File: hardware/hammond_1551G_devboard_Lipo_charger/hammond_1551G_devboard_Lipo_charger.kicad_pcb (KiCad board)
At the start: 4 copper layers, 44 x 29 mm, 25 parts, among them J1 DevBoardDigital, J2 DevBoardAnalog, J3 Battery_2pin, J4 DevBoardUartInput, J5 JTAG_2X05, Q1 Q_NMOS_GSD, U1 MCP1702-MB, U2 power_joiner_2_nets, U3 power_joiner_2_nets, U4 power_joiner_2_nets, U5 power_joiner_2_nets, U6 MCP738312-OT

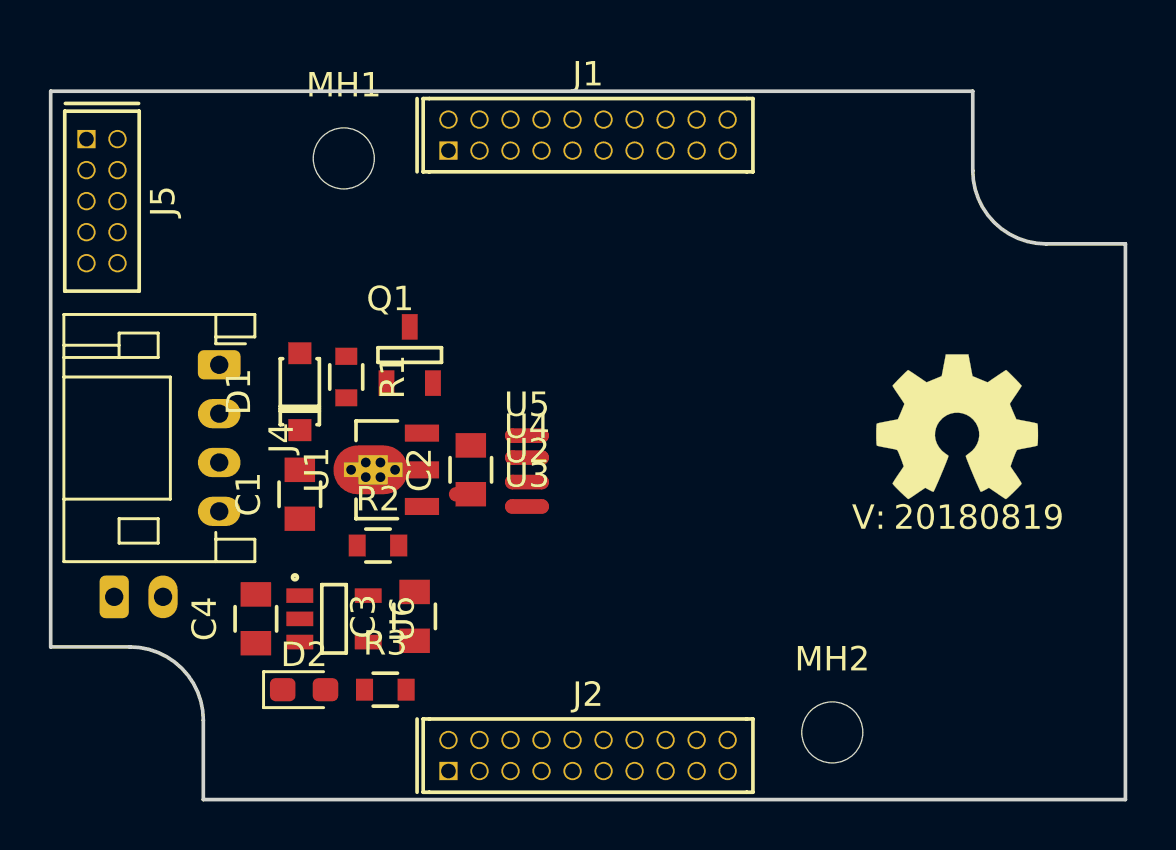
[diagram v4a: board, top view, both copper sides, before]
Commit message: further placement/layout, included newer PCB library
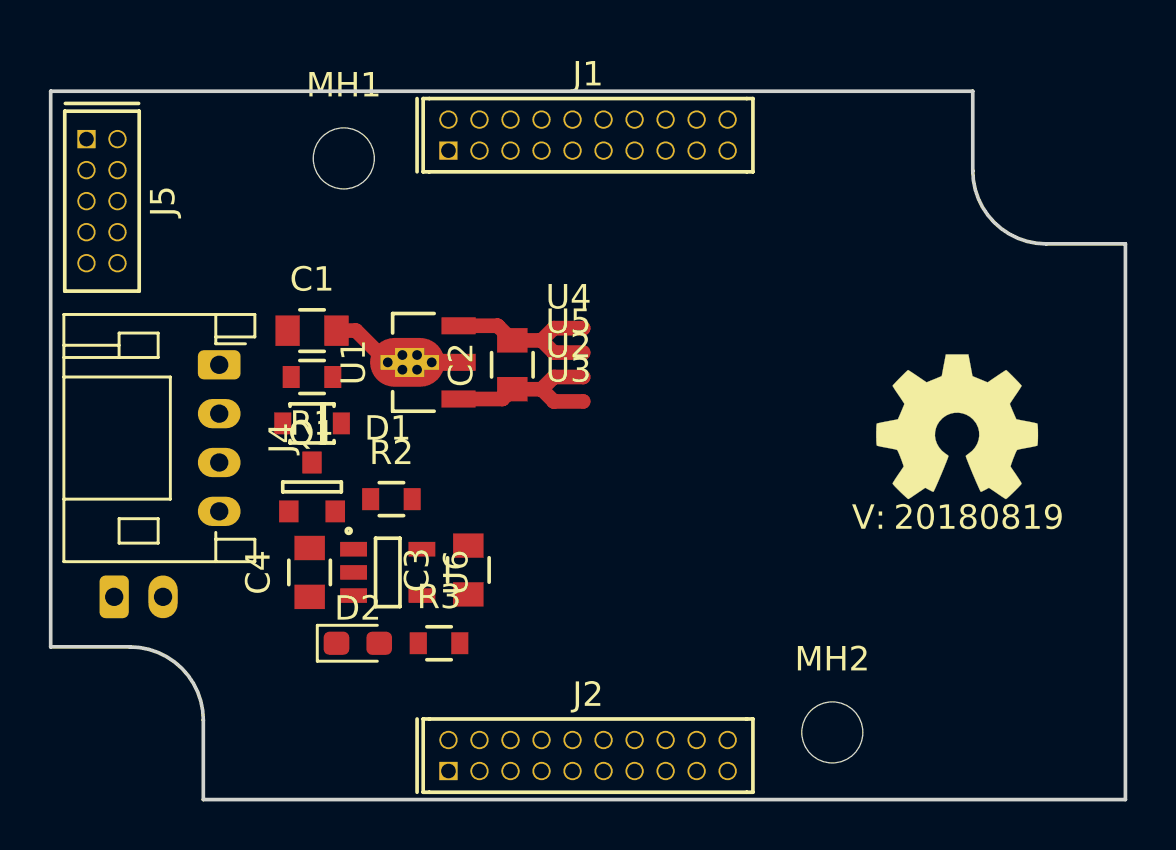
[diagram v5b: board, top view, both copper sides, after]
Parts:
- D1: footprint SquantorDiodes:SOD-123 -> SquantorDiodes:SOD_323_onsemi
- Q1: footprint SquantorIC:SOT23-3-Microchip-TT -> SquantorIC:SOT23-3
- moved Q1 6.72 mm to (49.0, 164.5)
- moved C1 6.72 mm to (49.0, 158.1), turned to 0 degrees
- moved U4 5.57 mm to (59.5, 158.0)
- moved U1 4.65 mm to (55.0, 159.4)
- moved C2 4.62 mm to (57.2, 159.5)
- moved U2 4.62 mm to (59.5, 160.0)
- moved U3 4.62 mm to (59.5, 161.0)
- moved U5 3.80 mm to (59.5, 159.0)
- moved D2 2.91 mm to (50.9, 170.9)
- moved R3 2.91 mm to (54.2, 170.9)
- moved U6 2.91 mm to (52.1, 168.0)
- moved C3 2.91 mm to (55.4, 167.9)
- moved C4 2.91 mm to (48.9, 168.0)
- moved R2 1.98 mm to (52.2, 165.0)
- moved R1 1.40 mm to (49.0, 160.0), turned to 180 degrees
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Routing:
- net Net-(C2-Pad2): track 0.00 -> 5.06 mm
- net Net-(C1-Pad2): track 0.00 -> 4.74 mm
- net GND: track 0.60 -> 4.98 mm

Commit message: completed layout, time for silk screen updates
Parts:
- moved U4 8.71 mm to (54.9, 165.4)
- moved U2 7.88 mm to (54.9, 166.4)
- moved U3 7.88 mm to (54.9, 167.4)
- moved U5 7.09 mm to (54.9, 164.4)
- moved R3 5.42 mm to (49.2, 173.0), turned to 90 degrees
- moved C2 5.33 mm to (53.1, 162.9), turned to 0 degrees
- moved C4 4.16 mm to (45.2, 169.9)
- moved D2 4.15 mm to (47.3, 173.0), turned to 270 degrees
- moved R2 4.07 mm to (48.7, 167.0), turned to 180 degrees
- moved C3 3.99 mm to (51.7, 169.4)
- moved U6 3.90 mm to (48.5, 169.5)
- moved U1 2.22 mm to (53.2, 160.7), turned to 0 degrees
- moved R1 0.30 mm to (48.7, 160.0)
- moved Q1 0.10 mm to (49.0, 164.4), turned to 90 degrees
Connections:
- net Net-(C1-Pad2) renamed /VREG
- J5 pad 1: GND -> VSS
- J5 pad 3: GND -> VSS
- J5 pad 5: GND -> VSS
- J5 pad 9: GND -> VSS
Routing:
- net +BATT: track 0.00 -> 36.1 mm, vias 0 -> 2
- net VBUS: track 0.00 -> 29.4 mm
- net GND: track 4.98 -> 24.5 mm, vias 0 -> 2
- net VDD: track 0.00 -> 17.0 mm
- net VDDA: track 0.00 -> 11.9 mm, vias 0 -> 1
- net VSSA: track 0.00 -> 11.3 mm
- net /VREG: track 4.74 -> 11.1 mm
- net Net-(D2-Pad1): track 0.00 -> 4.98 mm
- net Net-(J4-Pad3): track 0.00 -> 4.25 mm
- net VSS: track 0.00 -> 4.07 mm, vias 0 -> 1
- net Net-(D2-Pad2): track 0.00 -> 1.91 mm
- net Net-(R2-Pad1): track 0.00 -> 1.69 mm
- added copper zone on B.Cu, net /VREG
- added copper zone on B.Cu, net GND
- added copper zone on B.Cu, net VSS
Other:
- copper layers 4 -> 2
- net class Default: clearance 0.127 -> 0.1527; trace_width 0.127 -> 0.1527
- rule trace_clearance: 0.127 -> 0.1527
- rule trace_min: 0.127 -> 0.1524

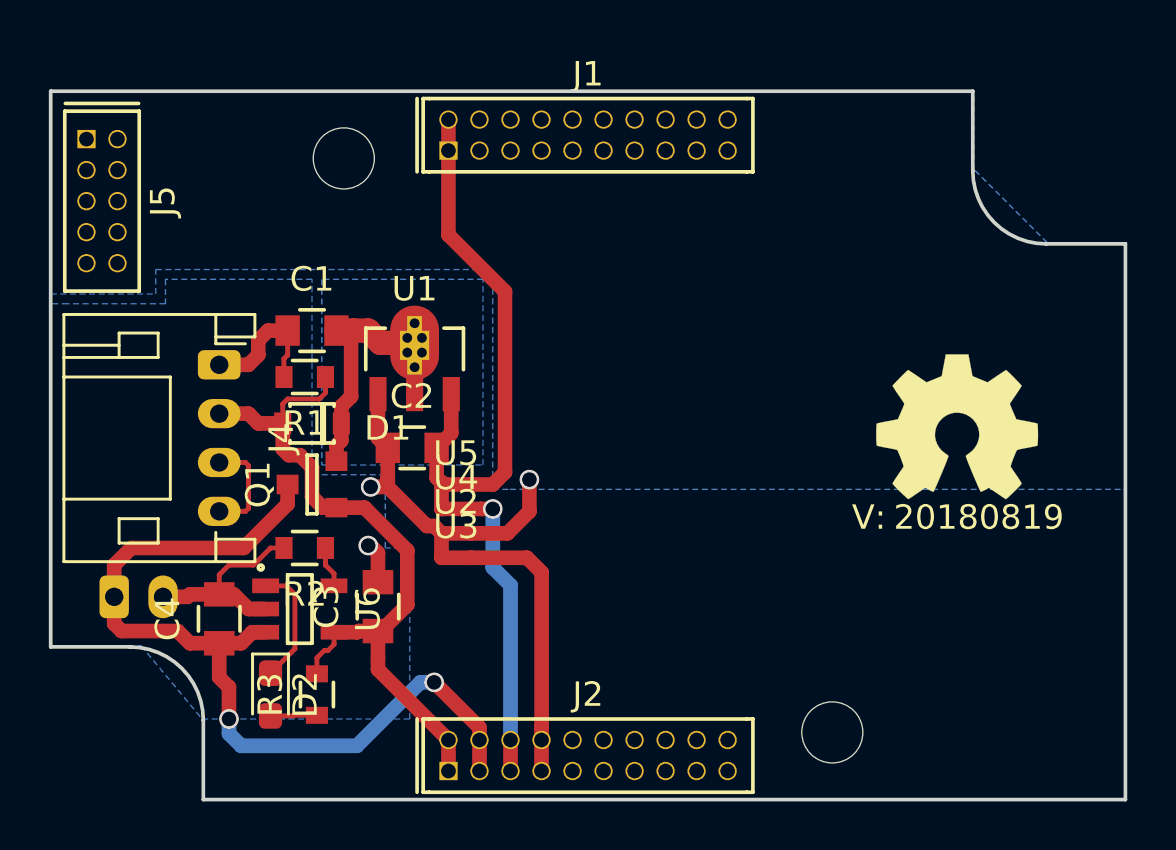
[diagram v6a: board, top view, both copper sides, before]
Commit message: replaced JST PH connectors by SMD variants so they stack better, needed to redo layout altough :(
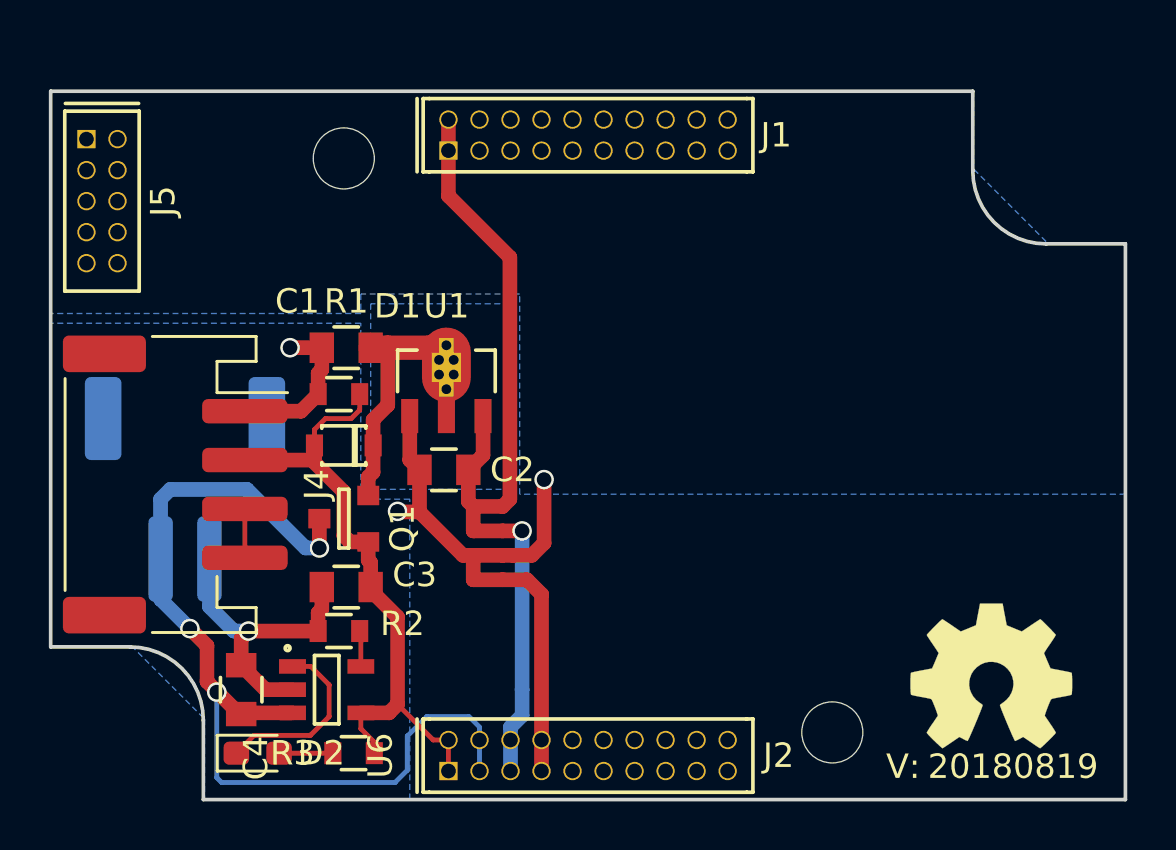
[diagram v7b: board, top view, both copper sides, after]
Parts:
- J3: footprint Connector_JST:JST_PH_S2B-PH-K_1x02_P2.00mm_Horizontal -> Connector_JST:JST_PH_S2B-PH-SM4-TB_1x02-1MP_P2.00mm_Horizontal
- J4: footprint Connector_JST:JST_PH_S4B-PH-K_1x04_P2.00mm_Horizontal -> Connector_JST:JST_PH_S4B-PH-SM4-TB_1x04-1MP_P2.00mm_Horizontal
- moved N2 10.3 mm to (78.1, 176.1)
- moved N1 10.3 mm to (76.8, 172.2)
- moved J3 5.27 mm to (43.8, 164.6)
- moved J4 5.22 mm to (43.4, 164.4)
- moved R2 3.68 mm to (50.1, 170.4)
- moved U6 3.48 mm to (49.6, 172.8)
- moved C4 3.04 mm to (46.1, 172.8)
- moved R3 2.83 mm to (50.7, 175.4), turned to 0 degrees
- moved D2 2.46 mm to (46.8, 175.4), turned to 0 degrees
- moved Q1 1.91 mm to (50.3, 165.8)
- moved U2 1.58 mm to (56.2, 167.3)
- moved U3 1.58 mm to (56.2, 168.3)
- moved U4 1.58 mm to (56.2, 166.3)
- moved U5 1.58 mm to (56.2, 165.3)
- moved C2 1.58 mm to (54.4, 163.8)
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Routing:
- net GND: track 24.5 -> 28.2 mm, vias 2 -> 3
- net +BATT: track 36.1 -> 39.5 mm, vias 2 -> 3
- net VBUS: track 29.4 -> 26.2 mm
- net Net-(D2-Pad1): track 4.98 -> 7.53 mm
- net Net-(J4-Pad3): track 4.25 -> 2.00 mm
- net VSSA: track 11.3 -> 9.08 mm
- net VDDA: track 11.9 -> 10.8 mm
- net Net-(D2-Pad2): track 1.91 -> 2.48 mm

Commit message: finished layout of an additional JTAG connection
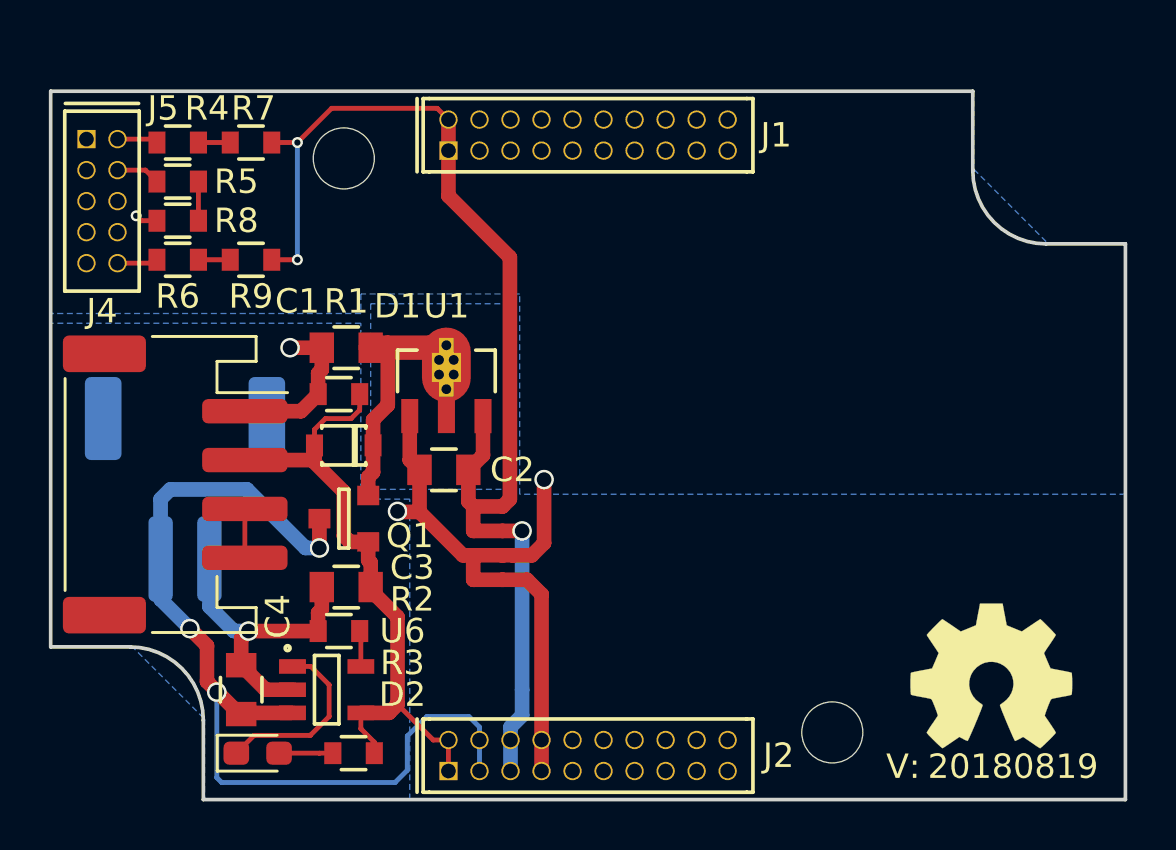
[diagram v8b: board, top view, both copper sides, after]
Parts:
- added R4: 100, SquantorRcl:R_0603_hand, F.Cu at (43.5, 150.4)
- added R5: 100, SquantorRcl:R_0603_hand, F.Cu at (43.5, 152.0)
- added R6: 100, SquantorRcl:R_0603_hand, F.Cu at (43.5, 155.2)
- added R7: 100k, SquantorRcl:R_0603_hand, F.Cu at (46.5, 150.4)
- added R8: 100k, SquantorRcl:R_0603_hand, F.Cu at (43.5, 153.6)
- added R9: 100k, SquantorRcl:R_0603_hand, F.Cu at (46.5, 155.2)
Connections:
- J5 pad 10: (no net) -> Net-(J5-Pad10)
- J5 pad 2: (no net) -> Net-(J5-Pad2)
- J5 pad 4: (no net) -> Net-(J5-Pad4)
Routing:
- net VDD: track 17.0 -> 30.9 mm, vias 0 -> 2
- net Net-(J5-Pad4): track 0.00 -> 1.81 mm
- net Net-(J5-Pad2): track 0.00 -> 1.67 mm
- net Net-(J5-Pad10): track 0.00 -> 1.67 mm
- net /TCK: track 0.00 -> 1.60 mm
- net /TMS: track 0.00 -> 1.30 mm
- net /RESET: track 0.00 -> 1.30 mm
- net VSS: track 4.51 -> 5.44 mm, vias 1 -> 2
